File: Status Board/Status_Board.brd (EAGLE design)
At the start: 172.7 x 55.9 mm, 47 parts

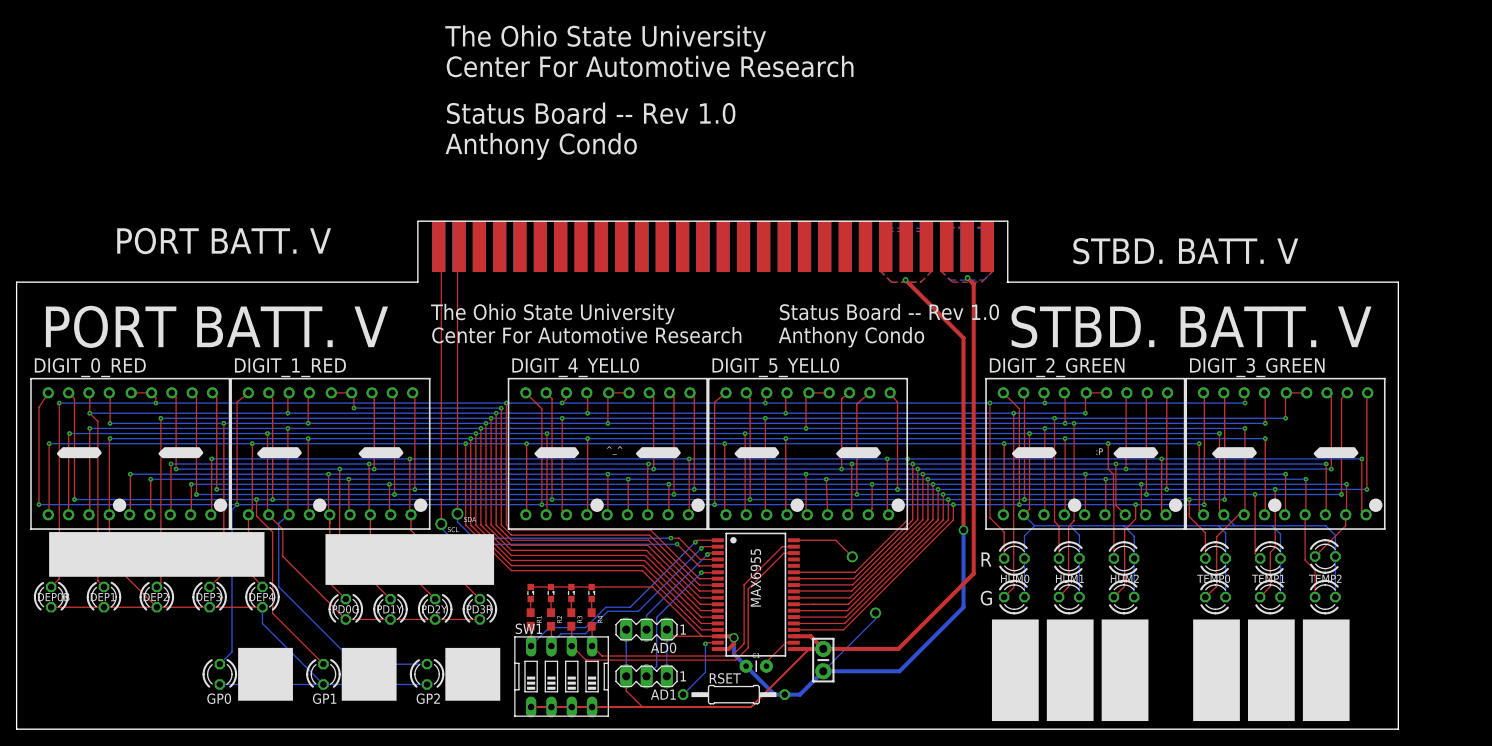
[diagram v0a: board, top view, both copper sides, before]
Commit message: Added Final Bulk Decoupling cap, updated lables, Gerber files are not updated to reflect new cap yet.
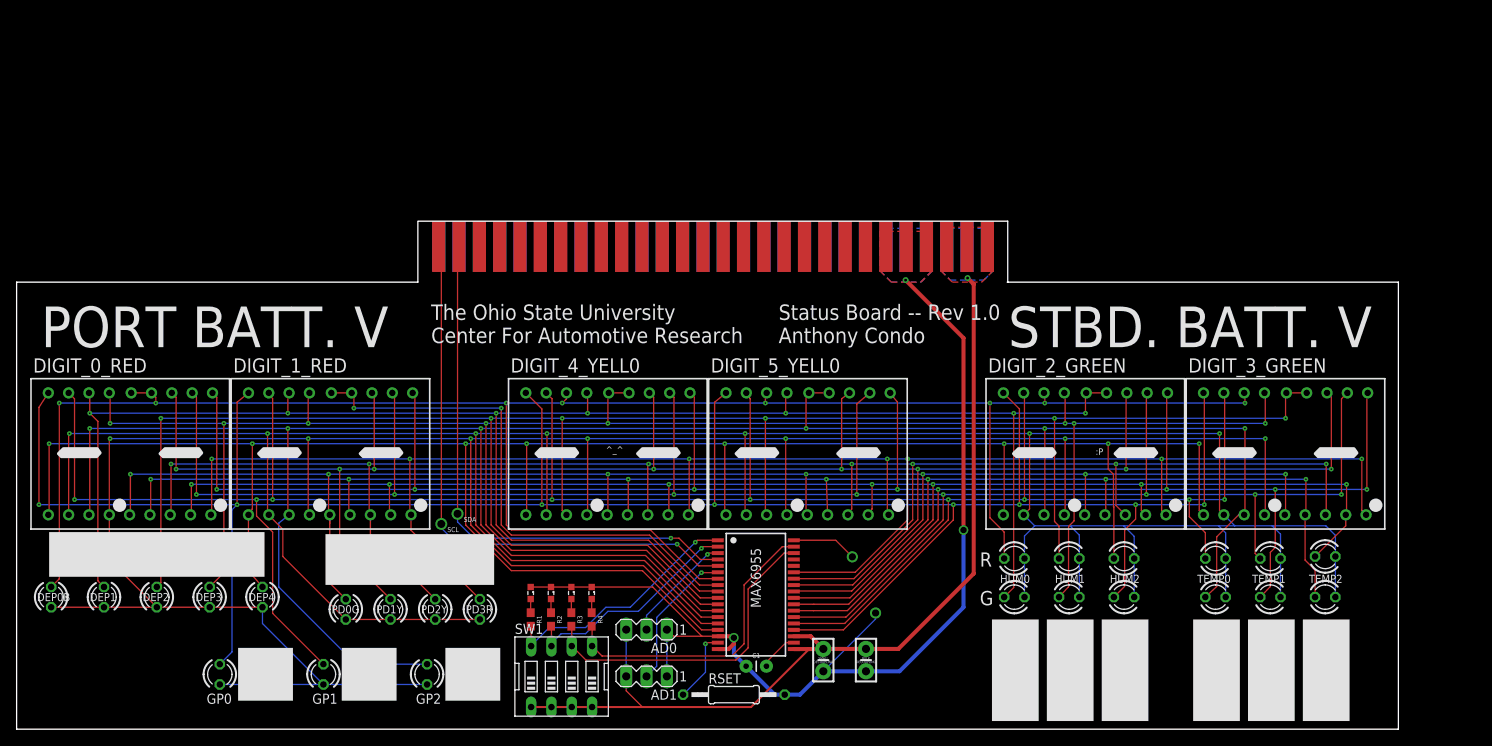
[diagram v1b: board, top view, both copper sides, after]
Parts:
- added BULK: F, SparkFun-Capacitors:CAP-PTH-SMALL-KIT
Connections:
- net GND: now also BULK.2
- net VCC: now also BULK.1
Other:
- board text added: "BULK DECOUPLING"
- board text added: "SMALL DECOUPLING"
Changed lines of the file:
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@@
 <text x="134.874" y="41.91" size="0.8128" layer="25">:P</text>
 <text x="14.478" y="40.894" size="0.8128" layer="25">&gt;:-}</text>
-<text x="53.594" y="89.154" size="2.54" layer="25">The Ohio State University
-Center For Automotive Research</text>
-<text x="53.594" y="79.502" size="2.54" layer="25">Status Board -- Rev 1.0
-Anthony Condo</text>
-<text x="12.192" y="67.056" size="3.175" layer="25">PORT BATT. V</text>
-<text x="131.826" y="65.786" size="3.175" layer="25">STBD. BATT. V</text>
 <text x="51.816" y="55.88" size="1.9304" layer="25">The Ohio State University
 Center For Automotive Research</text>
@@
 <text x="3.048" y="55.372" size="5.08" layer="25">PORT BATT. V</text>
 <text x="123.952" y="55.372" size="5.08" layer="25">STBD. BATT. V</text>
+<text x="100.838" y="16.256" size="0.3048" layer="25" align="center">SMALL
+DECOUPLING</text>
+<text x="106.172" y="16.256" size="0.3048" layer="25" align="center">BULK
+DECOUPLING</text>
 </plain>
 <attributes>
@@
 <attribute name="OC_NEWARK" value="unknown" x="78.74" y="14.224" size="1.778" layer="27" rot="R180" display="off"/>
 </element>
+<element name="BULK" library="SparkFun-Capacitors" package="CAP-PTH-SMALL-KIT" value="F" x="106.172" y="16.256" rot="R270">
+<attribute name="PROD_ID" value="CAP-08370" x="106.172" y="16.256" size="1.778" layer="27" rot="R270" display="off"/>
+</element>
 </elements>
 <signals>
@@
 <contactref element="C2" pad="2"/>
 <via x="118.364" y="32.512" extent="1-16" drill="0.8"/>
-<wire x1="100.838" y1="14.859" x2="110.363" y2="14.859" width="0.508" layer="16"/>
-<wire x1="110.363" y1="14.859" x2="118.364" y2="22.86" width="0.508" layer="16"/>
+<wire x1="118.364" y1="22.86" x2="110.363" y2="14.859" width="0.508" layer="16"/>
 <wire x1="118.364" y1="22.86" x2="118.364" y2="32.512" width="0.508" layer="16"/>
 <via x="89.662" y="19.05" extent="1-16" drill="0.8"/>
@@
 <wire x1="81.28" y1="20.066" x2="82.1112" y2="19.2348" width="0.1524" layer="1"/>
 <wire x1="82.1112" y1="19.2348" x2="85.6672" y2="19.2348" width="0.1524" layer="1"/>
+<contactref element="BULK" pad="2"/>
+<wire x1="110.363" y1="14.859" x2="106.172" y2="14.859" width="0.508" layer="16"/>
+<wire x1="106.172" y1="14.859" x2="100.838" y2="14.859" width="0.508" layer="16"/>
+<wire x1="113.7285" y1="67.945" x2="113.7285" y2="67.945" width="0" layer="19" extent="1-16"/>
+<wire x1="111.1885" y1="67.945" x2="113.7285" y2="67.945" width="0" layer="19" extent="1-1"/>
+<wire x1="111.1885" y1="67.945" x2="111.1885" y2="67.945" width="0" layer="19" extent="1-16"/>
+<wire x1="108.6485" y1="67.945" x2="111.1885" y2="67.945" width="0" layer="19" extent="1-1"/>
+<wire x1="108.6485" y1="67.945" x2="108.6485" y2="67.945" width="0" layer="19" extent="1-16"/>
+<wire x1="111.125" y1="63.754" x2="111.1885" y2="67.945" width="0" layer="19" extent="1-1"/>
 </signal>
 <signal name="O0">
@@
 <wire x1="97.1552" y1="17.6348" x2="99.06" y2="17.6348" width="0.508" layer="1"/>
 <wire x1="99.06" y1="17.6348" x2="100.8198" y2="17.6348" width="0.508" layer="1"/>
-<wire x1="100.838" y1="17.653" x2="110.2164625" y2="17.653" width="0.508" layer="1"/>
-<wire x1="119.634" y1="27.0705375" x2="110.2164625" y2="17.653" width="0.508" layer="1"/>
+<wire x1="110.2164625" y1="17.653" x2="119.634" y2="27.0705375" width="0.508" layer="1"/>
 <wire x1="118.872" y1="64.008" x2="119.634" y2="63.246" width="0.508" layer="1"/>
 <wire x1="119.634" y1="63.246" x2="119.634" y2="27.0705375" width="0.508" layer="1"/>
@@
 <wire x1="76.2" y1="12.4206" x2="78.232" y2="10.3886" width="0.1524" layer="1"/>
 <wire x1="76.2" y1="14.224" x2="76.2" y2="20.066" width="0.1524" layer="16"/>
+<contactref element="BULK" pad="1"/>
+<wire x1="100.838" y1="17.653" x2="106.172" y2="17.653" width="0.508" layer="1"/>
+<wire x1="106.172" y1="17.653" x2="110.2164625" y2="17.653" width="0.508" layer="1"/>
+<wire x1="121.3485" y1="67.945" x2="121.3485" y2="67.945" width="0" layer="19" extent="1-16"/>
+<wire x1="118.8085" y1="67.945" x2="121.3485" y2="67.945" width="0" layer="19" extent="1-1"/>
+<wire x1="118.8085" y1="67.945" x2="118.8085" y2="67.945" width="0" layer="19" extent="1-16"/>
+<wire x1="116.2685" y1="67.945" x2="118.8085" y2="67.945" width="0" layer="19" extent="1-1"/>
+<wire x1="116.2685" y1="67.945" x2="116.2685" y2="67.945" width="0" layer="19" extent="1-16"/>
+<wire x1="118.872" y1="64.008" x2="118.8085" y2="67.945" width="0" layer="19" extent="1-1"/>
 </signal>
 <signal name="O1">
